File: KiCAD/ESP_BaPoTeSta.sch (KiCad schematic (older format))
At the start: 13 parts, among them P1 CONN_01X03, SW1 SW_PUSH, SW2 SW_PUSH, U1 MCP1754ST-3302E/MB, U2 ESP-12, U3 DS18B20

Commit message: ENH: Finish board
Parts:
- removed BT1: 4.8V, symbol Battery
- added C1, C2: 1u, Capacitors_ThroughHole:C_Radial_D5_L11_P2, symbol CP_Small
- added P2: BattHdr, Pin_Headers:Pin_Header_Angled_1x02, symbol CONN_01X02
- added R7: 4k7, Resistors_ThroughHole:Resistor_Horizontal_RM10mm, symbol R
- P1: value CONN_01X03 -> ProgHdr; footprint (none) -> Pin_Headers:Pin_Header_Straight_1x03
- R1: value R -> 68k; footprint (none) -> Resistors_ThroughHole:Resistor_Horizontal_RM10mm
- R2, R3, R4, R5, R6: value R -> 10k; footprint (none) -> Resistors_ThroughHole:Resistor_Horizontal_RM10mm
- SW1: value SW_PUSH -> Upload; footprint (none) -> Buttons_Switches_ThroughHole:SW_PUSH_SMALL
- SW2: value SW_PUSH -> Reset; footprint (none) -> Buttons_Switches_ThroughHole:SW_PUSH_SMALL
- U1: value MCP1754ST-3302E/MB -> MCP1700-3302E/TO; footprint (none) -> TO_SOT_Packages_THT:TO-92_Inline_Wide
- U2: footprint (none) -> ESP8266:ESP-12
- U3: footprint (none) -> TO_SOT_Packages_THT:TO-92_Inline_Wide
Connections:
- net labels added: +BATT, 1Wire, Pwr1W
- net labels removed: 1W
- wire segments 31 -> 40
- no-connect marks 5 -> 4
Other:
- moved on the sheet: SW1
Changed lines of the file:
@@
 P 3650 2100
 F 0 "U1" H 3750 1950 50  0000 C CNN
-F 1 "MCP1754ST-3302E/MB" H 3650 2250 50  0000 C CNN
-F 2 "" H 3650 2100 50  0000 C CNN
+F 1 "MCP1700-3302E/TO" H 3650 2250 50  0000 C CNN
+F 2 "TO_SOT_Packages_THT:TO-92_Inline_Wide" H 3650 2100 50  0001 C CNN
 F 3 "" H 3650 2100 50  0000 C CNN
 	1    3650 2100
@@
 F 0 "U2" H 5850 2900 50  0000 C CNN
 F 1 "ESP-12" H 5850 3100 50  0000 C CNN
-F 2 "" H 5850 3000 50  0001 C CNN
+F 2 "ESP8266:ESP-12" H 5850 3000 50  0001 C CNN
 F 3 "" H 5850 3000 50  0001 C CNN
 	1    5850 3000
@@
 F 0 "U3" H 8150 3300 50  0000 C CNN
 F 1 "DS18B20" H 8300 2800 50  0000 C CNN
-F 2 "" H 8150 3300 50  0000 C CNN
+F 2 "TO_SOT_Packages_THT:TO-92_Inline_Wide" H 8150 3300 50  0001 C CNN
 F 3 "" H 8150 3300 50  0000 C CNN
 	1    8300 3050
@@
 U 1 1 5662879A
 P 7100 2950
-F 0 "R4" V 7180 2950 50  0000 C CNN
-F 1 "R" V 7100 2950 50  0000 C CNN
-F 2 "" V 7030 2950 50  0000 C CNN
+F 0 "R4" V 7000 2900 50  0000 C CNN
+F 1 "10k" V 7100 2950 50  0000 C CNN
+F 2 "Resistors_ThroughHole:Resistor_Horizontal_RM10mm" V 7030 2950 50  0001 C CNN
 F 3 "" H 7100 2950 50  0000 C CNN
 	1    7100 2950
@@
 P 7300 3050
 F 0 "R5" V 7380 3050 50  0000 C CNN
-F 1 "R" V 7300 3050 50  0000 C CNN
-F 2 "" V 7230 3050 50  0000 C CNN
+F 1 "10k" V 7300 3050 50  0000 C CNN
+F 2 "Resistors_ThroughHole:Resistor_Horizontal_RM10mm" V 7230 3050 50  0001 C CNN
 F 3 "" H 7300 3050 50  0000 C CNN
 	1    7300 3050
@@
 P 7550 3450
 F 0 "R6" V 7630 3450 50  0000 C CNN
-F 1 "R" V 7550 3450 50  0000 C CNN
-F 2 "" V 7480 3450 50  0000 C CNN
+F 1 "10k" V 7550 3450 50  0000 C CNN
+F 2 "Resistors_ThroughHole:Resistor_Horizontal_RM10mm" V 7480 3450 50  0001 C CNN
 F 3 "" H 7550 3450 50  0000 C CNN
 	1    7550 3450
@@
 P 4600 2750
 F 0 "R3" V 4680 2750 50  0000 C CNN
-F 1 "R" V 4600 2750 50  0000 C CNN
-F 2 "" V 4530 2750 50  0000 C CNN
+F 1 "10k" V 4600 2750 50  0000 C CNN
+F 2 "Resistors_ThroughHole:Resistor_Horizontal_RM10mm" V 4530 2750 50  0001 C CNN
 F 3 "" H 4600 2750 50  0000 C CNN
 	1    4600 2750
@@
 P 7550 3000
 F 0 "SW2" H 7700 3110 50  0000 C CNN
-F 1 "SW_PUSH" H 7550 2920 50  0000 C CNN
-F 2 "" H 7550 3000 50  0000 C CNN
+F 1 "Reset" H 7550 2920 50  0000 C CNN
+F 2 "Buttons_Switches_ThroughHole:SW_PUSH_SMALL" H 7550 3000 50  0001 C CNN
 F 3 "" H 7550 3000 50  0000 C CNN
 	1    7550 3000
@@
 L SW_PUSH SW1
 U 1 1 56628BAD
-P 7300 3500
-F 0 "SW1" H 7450 3610 50  0000 C CNN
-F 1 "SW_PUSH" H 7300 3420 50  0000 C CNN
-F 2 "" H 7300 3500 50  0000 C CNN
-F 3 "" H 7300 3500 50  0000 C CNN
-	1    7300 3500
+P 7100 3550
+F 0 "SW1" H 7250 3660 50  0000 C CNN
+F 1 "Upload" H 7100 3470 50  0000 C CNN
+F 2 "Buttons_Switches_ThroughHole:SW_PUSH_SMALL" H 7100 3550 50  0001 C CNN
+F 3 "" H 7100 3550 50  0000 C CNN
+	1    7100 3550
 	0    1    1    0
 $EndComp
@@
 P 2950 2250
 F 0 "R1" V 3030 2250 50  0000 C CNN
-F 1 "R" V 2950 2250 50  0000 C CNN
-F 2 "" V 2880 2250 50  0000 C CNN
+F 1 "68k" V 2950 2250 50  0000 C CNN
+F 2 "Resistors_ThroughHole:Resistor_Horizontal_RM10mm" V 2880 2250 50  0001 C CNN
 F 3 "" H 2950 2250 50  0000 C CNN
 	1    2950 2250
@@
 P 2950 2750
 F 0 "R2" V 3030 2750 50  0000 C CNN
-F 1 "R" V 2950 2750 50  0000 C CNN
-F 2 "" V 2880 2750 50  0000 C CNN
+F 1 "10k" V 2950 2750 50  0000 C CNN
+F 2 "Resistors_ThroughHole:Resistor_Horizontal_RM10mm" V 2880 2750 50  0001 C CNN
 F 3 "" H 2950 2750 50  0000 C CNN
 	1    2950 2750
 	1    0    0    -1
 $EndComp
-$Comp
-L Battery BT1
-U 1 1 56629A8B
-P 2350 2250
-F 0 "BT1" H 2450 2300 50  0000 L CNN
-F 1 "4.8V" H 2450 2200 50  0000 L CNN
-F 2 "" V 2350 2290 50  0000 C CNN
-F 3 "" V 2350 2290 50  0000 C CNN
-	1    2350 2250
-	1    0    0    -1
-$EndComp
-Text Label 4950 3300 0    60   ~ 0
-1W
-Text Label 8000 3050 0    60   ~ 0
-1W
+Text Label 4950 3300 2    60   ~ 0
+1Wire
+Text Label 8000 3050 2    60   ~ 0
+1Wire
 Wire Wire Line
 	6750 3300 7550 3300
@@
 Wire Wire Line
 	6750 3200 7300 3200
-Connection ~ 7300 3200
 Connection ~ 7550 3300
 Wire Wire Line
 	4600 2900 4950 2900
 Wire Wire Line
-	4600 2600 4600 2100
-Wire Wire Line
-	3950 2100 8000 2100
+	4600 2100 4600 2600
 Wire Wire Line
 	7100 2100 7100 2800
@@
 Wire Wire Line
 	7550 3900 7550 3600
-Wire Wire Line
-	7300 3900 7300 3800
 Connection ~ 7550 3900
-Connection ~ 7300 3900
 Wire Wire Line
 	4950 2700 4800 2700
@@
 	2950 2400 2950 2600
 Connection ~ 2950 2100
-Wire Wire Line
-	2350 2400 2350 3000
 Connection ~ 2950 3000
 Connection ~ 2950 2500
@@
 	4700 2800 4700 2500
 Wire Wire Line
-	8000 2100 8000 2950
-Connection ~ 7550 2100
-Wire Wire Line
 	8000 3900 8000 3150
 NoConn ~ 4950 3000
-NoConn ~ 4950 3100
 NoConn ~ 4950 3200
 NoConn ~ 6750 2900
-NoConn ~ 6750 3000
 $Comp
 L CONN_01X03 P1
@@
 P 6850 1450
 F 0 "P1" H 6850 1650 50  0000 C CNN
-F 1 "CONN_01X03" V 6950 1450 50  0000 C CNN
-F 2 "" H 6850 1450 50  0000 C CNN
+F 1 "ProgHdr" V 6950 1450 50  0000 C CNN
+F 2 "Pin_Headers:Pin_Header_Straight_1x03" H 6850 1450 50  0001 C CNN
 F 3 "" H 6850 1450 50  0000 C CNN
 	1    6850 1450
@@
 	6950 2800 6950 1650
 $Comp
-L GND #PWR05
+L GND #PWR03
 U 1 1 5662AF46
 P 6750 1750
-F 0 "#PWR05" H 6750 1500 50  0001 C CNN
+F 0 "#PWR03" H 6750 1500 50  0001 C CNN
 F 1 "GND" H 6750 1600 50  0000 C CNN
 F 2 "" H 6750 1750 50  0000 C CNN
@@
 Wire Wire Line
 	4700 2500 2950 2500
+$Comp
+L PWR_FLAG #FLG04
+U 1 1 5662B03F
+P 2350 2100
+F 0 "#FLG04" H 2350 2195 50  0001 C CNN
+F 1 "PWR_FLAG" H 2350 2280 50  0000 C CNN
+F 2 "" H 2350 2100 50  0000 C CNN
+F 3 "" H 2350 2100 50  0000 C CNN
+	1    2350 2100
+	1    0    0    -1
+$EndComp
+$Comp
+L PWR_FLAG #FLG05
+U 1 1 5662B14A
+P 2350 3000
+F 0 "#FLG05" H 2350 3095 50  0001 C CNN
+F 1 "PWR_FLAG" H 2350 3180 50  0000 C CNN
+F 2 "" H 2350 3000 50  0000 C CNN
+F 3 "" H 2350 3000 50  0000 C CNN
+	1    2350 3000
+	-1   0    0    1
+$EndComp
+$Comp
+L CP_Small C1
+U 1 1 5662B5FD
+P 3300 2300
+F 0 "C1" H 3310 2370 50  0000 L CNN
+F 1 "1u" H 3310 2220 50  0000 L CNN
+F 2 "Capacitors_ThroughHole:C_Radial_D5_L11_P2" H 3300 2300 50  0001 C CNN
+F 3 "" H 3300 2300 50  0000 C CNN
+	1    3300 2300
+	1    0    0    -1
+$EndComp
+$Comp
+L CP_Small C2
+U 1 1 5662B72E
+P 4000 2300
+F 0 "C2" H 4010 2370 50  0000 L CNN
+F 1 "1u" H 4010 2220 50  0000 L CNN
+F 2 "Capacitors_ThroughHole:C_Radial_D5_L11_P2" H 4000 2300 50  0001 C CNN
+F 3 "" H 4000 2300 50  0000 C CNN
+	1    4000 2300
+	1    0    0    -1
+$EndComp
+Wire Wire Line
+	4000 2200 4000 2100
+Connection ~ 4000 2100
+Wire Wire Line
+	4000 2400 4000 3900
+Connection ~ 4000 3900
+Wire Wire Line
+	3300 2200 3300 2100
+Connection ~ 3300 2100
+Wire Wire Line
+	3300 2400 3300 3000
+Connection ~ 3300 3000
+Wire Wire Line
+	7100 3100 7100 3250
+Wire Wire Line
+	7100 3850 7100 3900
+Connection ~ 7100 3900
+$Comp
+L R R7
+U 1 1 5662C4A4
+P 7750 2800
+F 0 "R7" V 7830 2800 50  0000 C CNN
+F 1 "4k7" V 7750 2800 50  0000 C CNN
+F 2 "Resistors_ThroughHole:Resistor_Horizontal_RM10mm" V 7680 2800 50  0001 C CNN
+F 3 "" H 7750 2800 50  0000 C CNN
+	1    7750 2800
+	1    0    0    -1
+$EndComp
+Wire Wire Line
+	7750 2950 7750 3050
+Wire Wire Line
+	7750 3050 8000 3050
+$Comp
+L CONN_01X02 P2
+U 1 1 5662C8D4
+P 2150 2550
+F 0 "P2" H 2150 2700 50  0000 C CNN
+F 1 "BattHdr" V 2250 2550 50  0000 C CNN
+F 2 "Pin_Headers:Pin_Header_Angled_1x02" H 2150 2550 50  0001 C CNN
+F 3 "" H 2150 2550 50  0000 C CNN
+	1    2150 2550
+	-1   0    0    1
+$EndComp
+Wire Wire Line
+	2350 2500 2350 2100
+Wire Wire Line
+	2350 2600 2350 3000
+$Comp
+L +BATT #PWR06
+U 1 1 5662D0E0
+P 2350 2100
+F 0 "#PWR06" H 2350 1950 50  0001 C CNN
+F 1 "+BATT" H 2350 2240 50  0000 C CNN
+F 2 "" H 2350 2100 50  0000 C CNN
+F 3 "" H 2350 2100 50  0000 C CNN
+	1    2350 2100
+	0    -1   -1   0
+$EndComp
+Wire Wire Line
+	3950 2100 7550 2100
+Text Label 4950 3100 2    60   ~ 0
+Pwr1W
+Wire Wire Line
+	7750 2650 8000 2650
+Wire Wire Line
+	8000 2650 8000 2950
+Text Label 8000 2650 0    60   ~ 0
+Pwr1W
+Connection ~ 8000 2650
+NoConn ~ 6750 3000
 $EndSCHEMATC

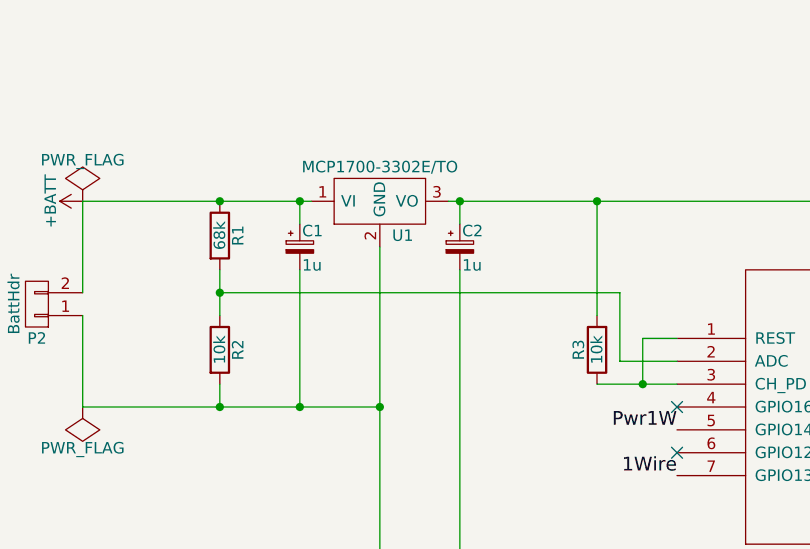
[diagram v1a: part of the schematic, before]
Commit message: TXT: "1u" -> ">=1u"
as bigger caps are also okay
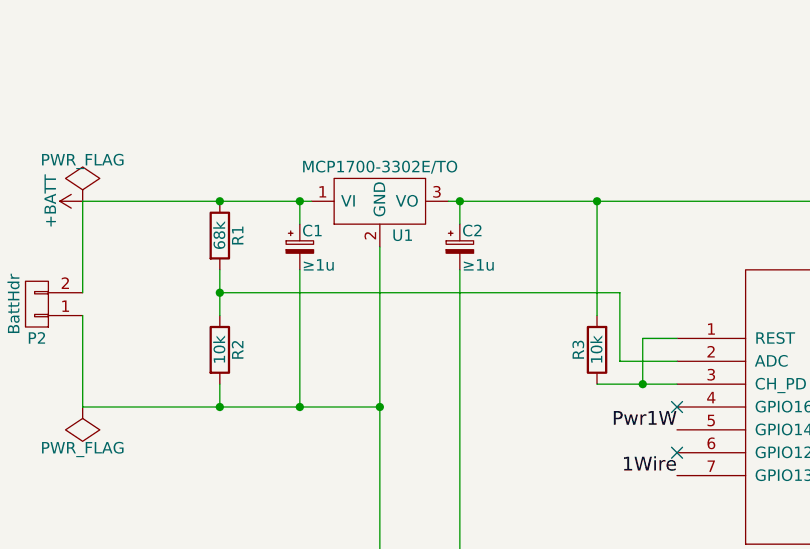
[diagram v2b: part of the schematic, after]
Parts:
- C1, C2: value 1u -> ≥1u
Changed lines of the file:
@@
 P 3300 2300
 F 0 "C1" H 3310 2370 50  0000 L CNN
-F 1 "1u" H 3310 2220 50  0000 L CNN
+F 1 "≥1u" H 3310 2220 50  0000 L CNN
 F 2 "Capacitors_ThroughHole:C_Radial_D5_L11_P2" H 3300 2300 50  0001 C CNN
 F 3 "" H 3300 2300 50  0000 C CNN
@@
 P 4000 2300
 F 0 "C2" H 4010 2370 50  0000 L CNN
-F 1 "1u" H 4010 2220 50  0000 L CNN
+F 1 "≥1u" H 4010 2220 50  0000 L CNN
 F 2 "Capacitors_ThroughHole:C_Radial_D5_L11_P2" H 4000 2300 50  0001 C CNN
 F 3 "" H 4000 2300 50  0000 C CNN

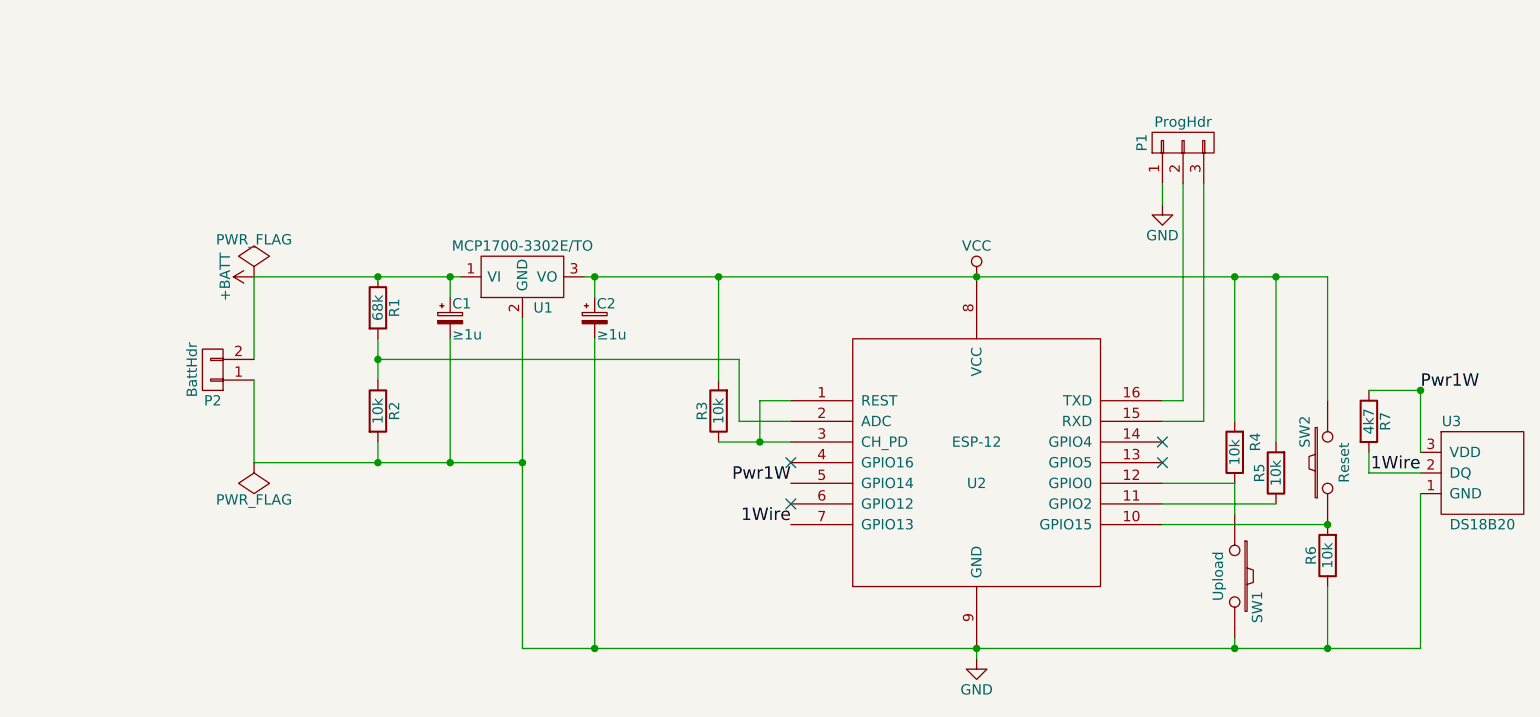
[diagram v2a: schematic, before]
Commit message: ENH: add Power header
might be useful
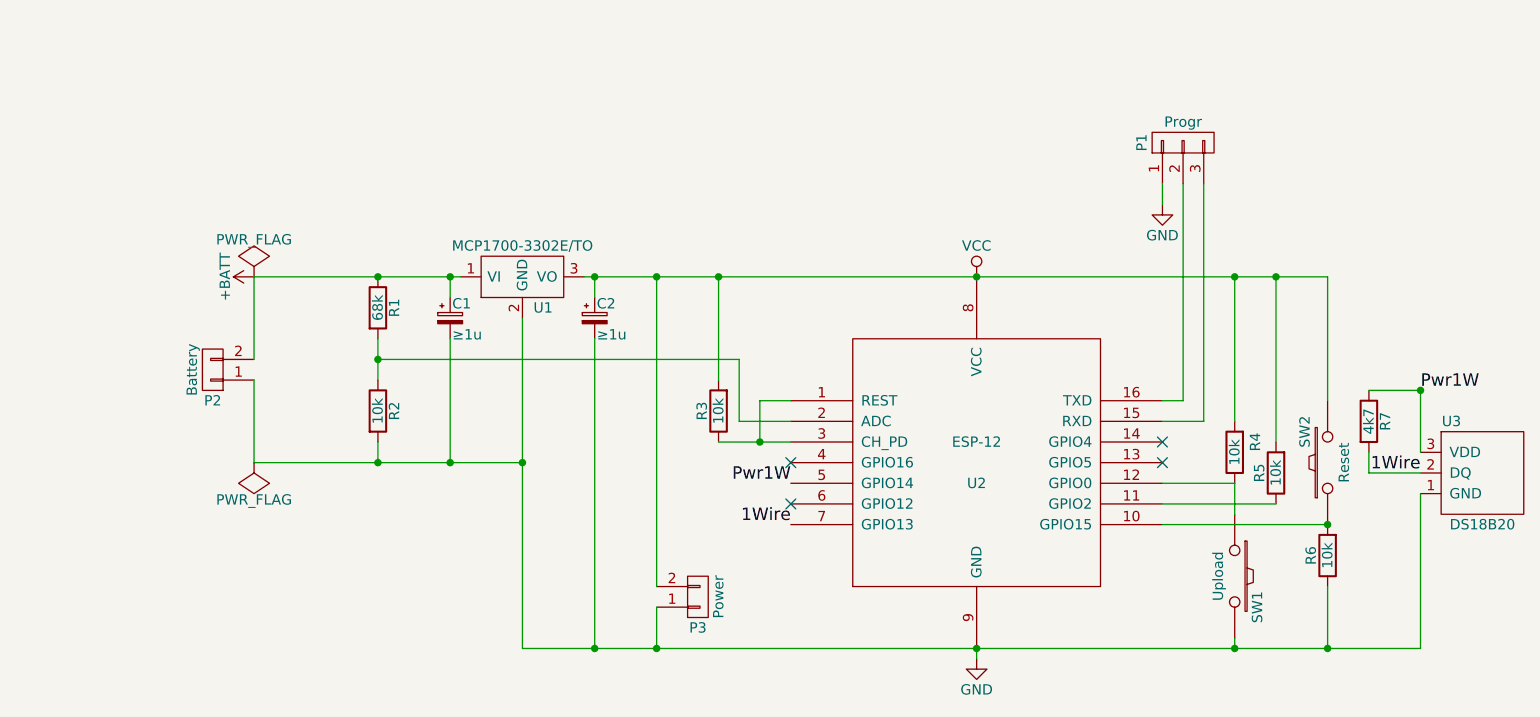
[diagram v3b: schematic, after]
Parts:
- added P3: Power, Pin_Headers:Pin_Header_Straight_1x02, symbol CONN_01X02
- P1: value ProgHdr -> Progr
- P2: value BattHdr -> Battery
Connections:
- net GND: now also P3.1 (P1)
- net VCC: now also P3.2 (P2)
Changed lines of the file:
@@
 P 6850 1450
 F 0 "P1" H 6850 1650 50  0000 C CNN
-F 1 "ProgHdr" V 6950 1450 50  0000 C CNN
+F 1 "Progr" V 6950 1450 50  0000 C CNN
 F 2 "Pin_Headers:Pin_Header_Straight_1x03" H 6850 1450 50  0001 C CNN
 F 3 "" H 6850 1450 50  0000 C CNN
@@
 P 2150 2550
 F 0 "P2" H 2150 2700 50  0000 C CNN
-F 1 "BattHdr" V 2250 2550 50  0000 C CNN
+F 1 "Battery" V 2250 2550 50  0000 C CNN
 F 2 "Pin_Headers:Pin_Header_Angled_1x02" H 2150 2550 50  0001 C CNN
 F 3 "" H 2150 2550 50  0000 C CNN
@@
 Connection ~ 8000 2650
 NoConn ~ 6750 3000
+$Comp
+L CONN_01X02 P3
+U 1 1 56659295
+P 4500 3650
+F 0 "P3" H 4500 3800 50  0000 C CNN
+F 1 "Power" V 4600 3650 50  0000 C CNN
+F 2 "Pin_Headers:Pin_Header_Straight_1x02" H 4500 3650 50  0001 C CNN
+F 3 "" H 4500 3650 50  0000 C CNN
+	1    4500 3650
+	1    0    0    1
+$EndComp
+Wire Wire Line
+	4300 3700 4300 3900
+Connection ~ 4300 3900
+Wire Wire Line
+	4300 3600 4300 2100
+Connection ~ 4300 2100
 $EndSCHEMATC

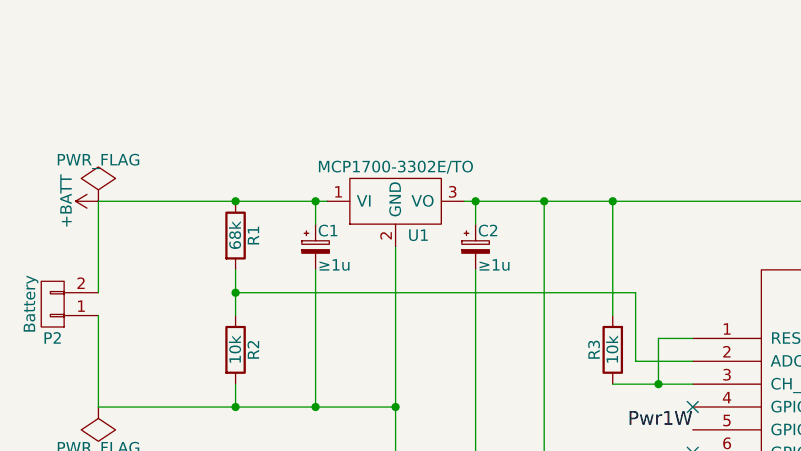
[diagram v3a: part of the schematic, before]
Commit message: TXT: improve labeling of MCP1700
drop "/TO" from name, so it fits better on the silk-screen
uppercase "IN" and "OUT" (as everything else is uppercase)
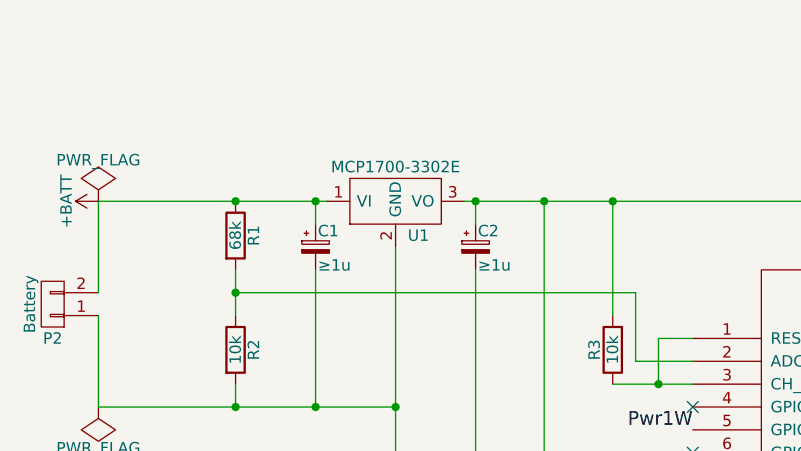
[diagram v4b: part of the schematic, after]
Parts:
- U1: value MCP1700-3302E/TO -> MCP1700-3302E
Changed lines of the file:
@@
 P 3650 2100
 F 0 "U1" H 3750 1950 50  0000 C CNN
-F 1 "MCP1700-3302E/TO" H 3650 2250 50  0000 C CNN
+F 1 "MCP1700-3302E" H 3650 2250 50  0000 C CNN
 F 2 "TO_SOT_Packages_THT:TO-92_Inline_Wide" H 3650 2100 50  0001 C CNN
 F 3 "" H 3650 2100 50  0000 C CNN
